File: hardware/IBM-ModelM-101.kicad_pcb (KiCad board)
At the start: 2 copper layers, 150 x 50 mm, 42 parts, among them J1 CONN-MOLEX-0670688000-USB-B, J2 KEYBOARD_ACTIVE_LINES, J3 KEYBOARD_INPUT_LINES, J4 CHASSIS_GROUND, J5 STATUS_LEDS, J6 DEBUG_FTDI, J7 JTAG, SW1 BOOT0, SW2 RESET, U1 TLV70233DBV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

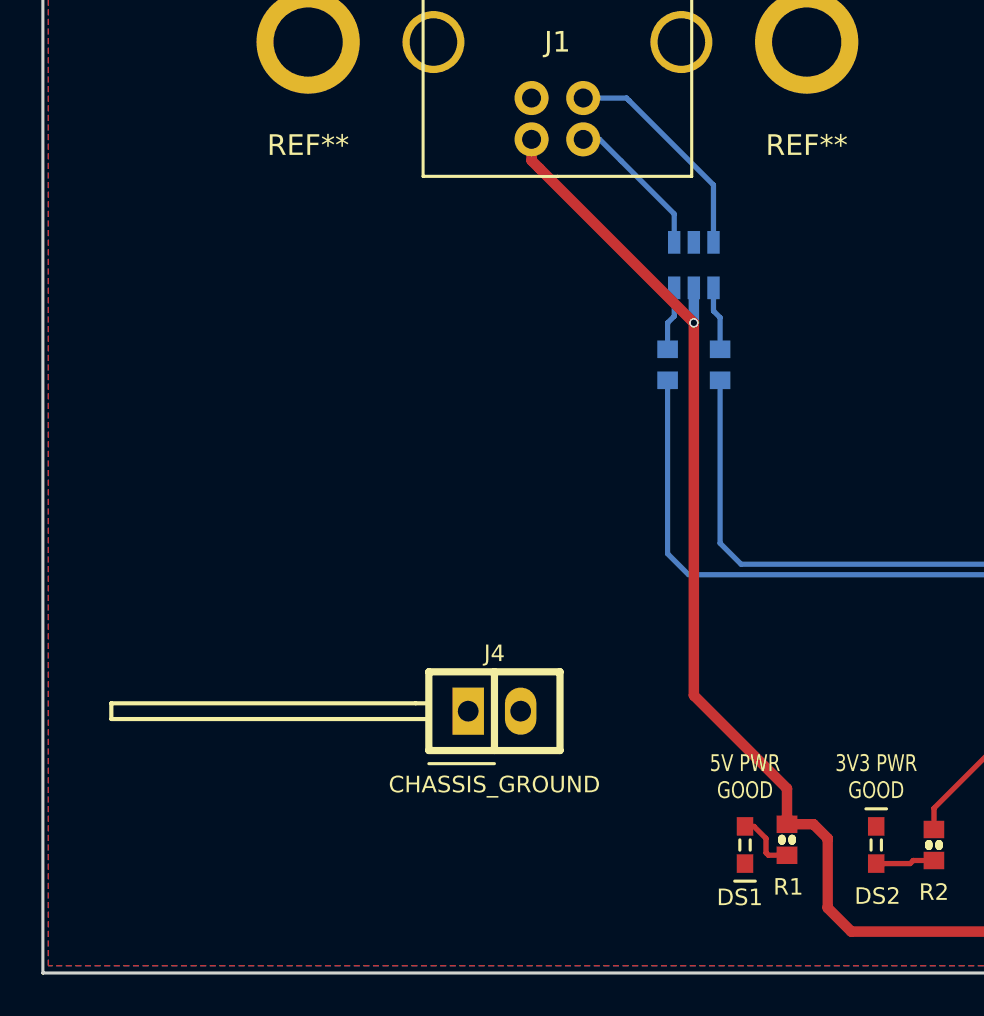
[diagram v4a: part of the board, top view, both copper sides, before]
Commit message: Updates + replaced tab header with correct footprint
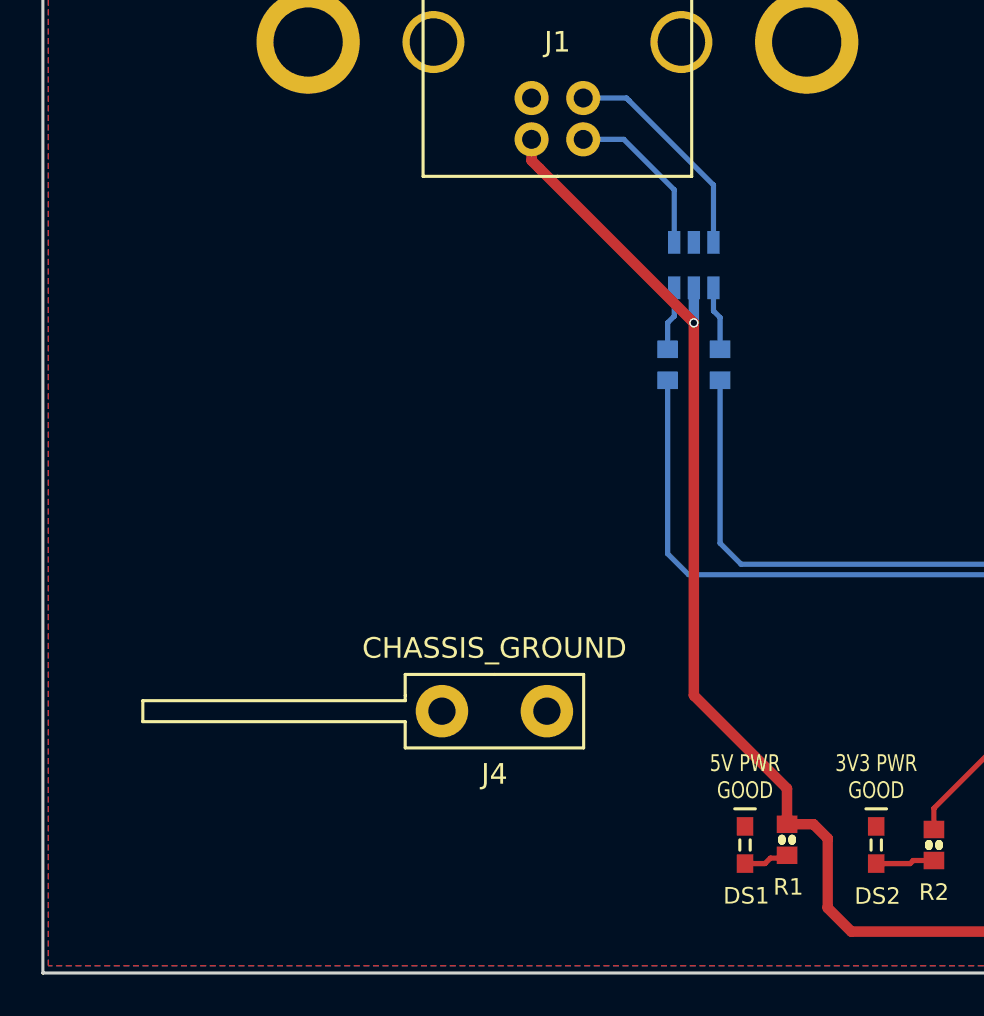
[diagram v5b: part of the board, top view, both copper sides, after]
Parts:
- J4: footprint conn-100mil:CONN-100MIL-M-1x2 -> conn-molex:CONN-MOLEX-0197134001-TAB
- turned DS1 to 270 degrees
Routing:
- net Net-(DS1-Pad2): track 3.02 -> 2.20 mm
- net Net-(DZ1-Pad1): track 7.27 -> 7.96 mm
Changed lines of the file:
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@@
     (links 128)
     (no_connects 1)
-    (area 85.003799 26.605199 235.153801 76.755201)
+    (area 85.003799 20.793999 235.153801 76.755201)
     (thickness 1.6)
-    (drawings 12)
-    (tracks 494)
+    (drawings 7)
+    (tracks 492)
     (zones 0)
     (modules 42)
@@
     (visible_elements 7FFFFFFF)
     (pcbplotparams
-      (layerselection 0x01030_80000001)
+      (layerselection 0x010f0_80000001)
       (usegerberextensions false)
       (excludeedgelayer true)
@@
   )
   (module smd-semi:LED-0603 (layer F.Cu)
-    (at 119.0625 70.485 90)
-    (fp_text reference DS1 (at -2.54 -0.254 180) (layer F.SilkS)
-      (effects (font (size 0.8 0.8) (thickness 0.15)))
-    )
-    (fp_text value 5V_PWR_GOOD (at -4.191 -1.4605 180) (layer F.Fab)
+    (at 119.0625 70.485 270)
+    (fp_text reference DS1 (at 2.4638 -0.0635 360) (layer F.SilkS)
+      (effects (font (size 0.8 0.8) (thickness 0.15)))
+    )
+    (fp_text value 5V_PWR_GOOD (at 4.2164 0.9779 360) (layer F.Fab)
       (effects (font (size 0.8 0.8) (thickness 0.15)))
     )
@@
     (fp_line (start 1.75 0.75) (end -1.75 0.75) (layer F.CrtYd) (width 0.15))
     (fp_line (start -1.75 0.75) (end -1.75 -0.75) (layer F.CrtYd) (width 0.15))
-    (pad 1 smd rect (at -0.89916 0 90) (size 0.89916 0.8001) (layers F.Cu F.Paste F.Mask)
-      (net 1 GND))
-    (pad 2 smd rect (at 0.89916 0 90) (size 0.89916 0.8001) (layers F.Cu F.Paste F.Mask)
+    (pad 1 smd rect (at -0.89916 0 270) (size 0.89916 0.8001) (layers F.Cu F.Paste F.Mask)
+      (net 1 GND))
+    (pad 2 smd rect (at 0.89916 0 270) (size 0.89916 0.8001) (layers F.Cu F.Paste F.Mask)
       (net 7 "Net-(DS1-Pad2)"))
     (model smd_leds/led_0603.wrl
@@
     )
   )
-  (module conn-100mil:CONN-100MIL-M-1x2 locked (layer F.Cu)
-    (at 106.934 64.008)
-    (fp_text reference J4 (at 0 -2.794) (layer F.SilkS)
-      (effects (font (size 0.8 0.8) (thickness 0.15)))
-    )
-    (fp_text value CHASSIS_GROUND (at 0 3.556) (layer F.SilkS)
-      (effects (font (size 0.8 0.8) (thickness 0.15)))
-    )
-    (fp_line (start -3.175 -1.905) (end 3.175 -1.905) (layer F.CrtYd) (width 0.15))
-    (fp_line (start 3.175 -1.905) (end 3.175 1.905) (layer F.CrtYd) (width 0.15))
-    (fp_line (start 3.175 1.905) (end -3.175 1.905) (layer F.CrtYd) (width 0.15))
-    (fp_line (start -3.175 1.905) (end -3.175 -1.905) (layer F.CrtYd) (width 0.15))
-    (fp_line (start -3.175 -1.905) (end 3.175 -1.905) (layer F.Fab) (width 0.15))
-    (fp_line (start 3.175 -1.905) (end 3.175 1.905) (layer F.Fab) (width 0.15))
-    (fp_line (start 3.175 1.905) (end -3.175 1.905) (layer F.Fab) (width 0.15))
-    (fp_line (start -3.175 1.905) (end -3.175 -1.905) (layer F.Fab) (width 0.15))
-    (fp_line (start -3.175 -1.905) (end 3.175 -1.905) (layer F.SilkS) (width 0.35))
-    (fp_line (start 3.175 -1.905) (end 3.175 1.905) (layer F.SilkS) (width 0.35))
-    (fp_line (start 3.175 1.905) (end -3.175 1.905) (layer F.SilkS) (width 0.35))
-    (fp_line (start -3.175 1.905) (end -3.175 -1.905) (layer F.SilkS) (width 0.35))
-    (fp_line (start 0 -1.905) (end 0 1.905) (layer F.SilkS) (width 0.35))
-    (fp_line (start 0 -1.905) (end 0 1.905) (layer F.Fab) (width 0.15))
-    (fp_line (start -3.175 2.54) (end 0 2.54) (layer F.SilkS) (width 0.15))
-    (pad 1 thru_hole rect (at -1.27 0) (size 1.524 2.286) (drill 1) (layers *.Cu *.Mask F.SilkS)
-      (net 1 GND))
-    (pad 2 thru_hole oval (at 1.27 0) (size 1.524 2.286) (drill 1) (layers *.Cu *.Mask F.SilkS)
-      (net 1 GND))
-    (model pin_strip/pin_strip_2.wrl
-      (at (xyz 0 0 0))
-      (scale (xyz 1 1 1))
-      (rotate (xyz 0 0 0))
-    )
-  )
   (module conn-100mil:CONN-100MIL-M-1x4-SHROUD (layer F.Cu)
     (at 225.79 53.89 270)
@@
   (module mech:PTH-3MM-PLUS (layer F.Cu)
     (at 122.047 31.623)
-    (fp_text reference REF** (at 0 5) (layer F.SilkS)
+    (fp_text reference REF** (at 0 5) (layer F.SilkS) hide
       (effects (font (size 1 1) (thickness 0.15)))
     )
@@
   (module mech:PTH-3MM-PLUS (layer F.Cu)
     (at 97.917 31.623)
-    (fp_text reference REF** (at 0 5) (layer F.SilkS)
+    (fp_text reference REF** (at 0 5) (layer F.SilkS) hide
       (effects (font (size 1 1) (thickness 0.15)))
     )
@@
       (net 3 +5V))
   )
+  (module conn-molex:CONN-MOLEX-0197134001-TAB locked (layer F.Cu)
+    (at 106.934 64.008)
+    (fp_text reference J4 (at 0 3.048) (layer F.SilkS)
+      (effects (font (size 1 1) (thickness 0.15)))
+    )
+    (fp_text value CHASSIS_GROUND (at 0 -3.048) (layer F.SilkS)
+      (effects (font (size 1 1) (thickness 0.15)))
+    )
+    (fp_line (start -4.318 -0.508) (end -17.018 -0.508) (layer F.SilkS) (width 0.15))
+    (fp_line (start -17.018 -0.508) (end -17.018 0.508) (layer F.SilkS) (width 0.15))
+    (fp_line (start -17.018 0.508) (end -4.318 0.508) (layer F.SilkS) (width 0.15))
+    (fp_line (start -4.318 -0.762) (end -4.318 -0.508) (layer F.SilkS) (width 0.15))
+    (fp_line (start 0 -1.778) (end -4.318 -1.778) (layer F.SilkS) (width 0.15))
+    (fp_line (start -4.318 -1.778) (end -4.318 -0.762) (layer F.SilkS) (width 0.15))
+    (fp_line (start -4.318 1.778) (end -4.318 0.508) (layer F.SilkS) (width 0.15))
+    (fp_line (start 0 -1.778) (end 4.318 -1.778) (layer F.SilkS) (width 0.15))
+    (fp_line (start 4.318 -1.778) (end 4.318 1.778) (layer F.SilkS) (width 0.15))
+    (fp_line (start 4.318 1.778) (end -4.318 1.778) (layer F.SilkS) (width 0.15))
+    (pad 1 thru_hole circle (at -2.54 0) (size 2.54 2.54) (drill 1.3208) (layers *.Cu *.Mask F.SilkS)
+      (net 1 GND))
+    (pad 2 thru_hole circle (at 2.54 0) (size 2.54 2.54) (drill 1.3208) (layers *.Cu *.Mask F.SilkS)
+      (net 1 GND))
+  )
   (gr_text "5V FROM\nJTAG\n" (at 162.6235 64.643) (layer F.SilkS)
     (effects (font (size 0.8128 0.889) (thickness 0.1524)))
@@
     (effects (font (size 0.8128 0.635) (thickness 0.1524)))
   )
-  (gr_line (start 103.124 64.389) (end 103.759 64.389) (angle 90) (layer F.SilkS) (width 0.2))
-  (gr_line (start 103.124 63.627) (end 103.759 63.627) (angle 90) (layer F.SilkS) (width 0.2))
-  (gr_line (start 103.124 63.627) (end 88.392 63.627) (angle 90) (layer F.SilkS) (width 0.2))
-  (gr_line (start 88.392 64.389) (end 103.124 64.389) (angle 90) (layer F.SilkS) (width 0.2))
-  (gr_line (start 88.392 63.627) (end 88.392 64.389) (angle 90) (layer F.SilkS) (width 0.2))
   (gr_line (start 85.0788 76.6802) (end 85.0788 26.6802) (angle 90) (layer Edge.Cuts) (width 0.15))
   (gr_line (start 235.0788 76.6802) (end 85.0788 76.6802) (angle 90) (layer Edge.Cuts) (width 0.15))
@@
   (segment (start 150.137 45.201) (end 149.987 45.351) (width 0.254) (layer F.Cu) (net 2))
   (segment (start 151.963 45.145) (end 152.019 45.201) (width 0.254) (layer F.Cu) (net 2))
-  (segment (start 108.732 36.333) (end 108.732 37.358) (width 0.508) (layer F.Cu) (net 3) (status 400000))
+  (segment (start 108.732 36.333) (end 108.732 37.358) (width 0.508) (layer F.Cu) (net 3))
   (segment (start 109.1184 37.7444) (end 116.586 45.212) (width 0.508) (layer F.Cu) (net 3))
   (segment (start 108.732 37.358) (end 109.1184 37.7444) (width 0.508) (layer F.Cu) (net 3))
@@
   (segment (start 176.022 60.706) (end 176.022 69.088) (width 0.254) (layer B.Cu) (net 6))
   (segment (start 176.022 60.706) (end 176.022 56.63) (width 0.254) (layer B.Cu) (net 6))
-  (segment (start 119.0625 69.58584) (end 119.49684 69.58584) (width 0.254) (layer F.Cu) (net 7))
-  (segment (start 120.1935 70.981) (end 121.0945 70.981) (width 0.254) (layer F.Cu) (net 7))
-  (segment (start 120.0785 70.866) (end 120.1935 70.981) (width 0.254) (layer F.Cu) (net 7))
-  (segment (start 120.0785 70.1675) (end 120.0785 70.866) (width 0.254) (layer F.Cu) (net 7))
-  (segment (start 119.49684 69.58584) (end 120.0785 70.1675) (width 0.254) (layer F.Cu) (net 7))
+  (segment (start 119.0625 71.38416) (end 120.03024 71.38416) (width 0.254) (layer F.Cu) (net 7))
+  (segment (start 120.2944 71.12) (end 120.9555 71.12) (width 0.254) (layer F.Cu) (net 7))
+  (segment (start 120.03024 71.38416) (end 120.2944 71.12) (width 0.254) (layer F.Cu) (net 7))
+  (segment (start 120.9555 71.12) (end 121.0945 70.981) (width 0.254) (layer F.Cu) (net 7))
   (segment (start 125.4125 71.38416) (end 127.05334 71.38416) (width 0.254) (layer F.Cu) (net 8))
   (segment (start 127.2025 71.235) (end 128.2065 71.235) (width 0.254) (layer F.Cu) (net 8))
   (segment (start 127.05334 71.38416) (end 127.2025 71.235) (width 0.254) (layer F.Cu) (net 8))
   (segment (start 125.26334 71.235) (end 125.4125 71.38416) (width 0.254) (layer F.Cu) (net 8))
-  (segment (start 111.232 36.333) (end 112.025 36.333) (width 0.254) (layer B.Cu) (net 9) (status C00000))
-  (segment (start 112.025 36.333) (end 113.0681 37.3761) (width 0.254) (layer B.Cu) (net 9) (status 400000))
-  (segment (start 115.636 39.944) (end 115.636 41.318) (width 0.254) (layer B.Cu) (net 9))
-  (segment (start 113.0681 37.3761) (end 115.636 39.944) (width 0.254) (layer B.Cu) (net 9))
+  (segment (start 115.636 41.318) (end 115.636 38.7756) (width 0.254) (layer B.Cu) (net 9))
+  (segment (start 113.1934 36.333) (end 111.232 36.333) (width 0.254) (layer B.Cu) (net 9))
+  (segment (start 115.636 38.7756) (end 113.1934 36.333) (width 0.254) (layer B.Cu) (net 9))
   (segment (start 111.232 34.333) (end 113.327 34.333) (width 0.254) (layer B.Cu) (net 10))
   (segment (start 113.454 34.46) (end 117.536 38.542) (width 0.254) (layer B.Cu) (net 10))

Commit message: Fixed unconnected pads + ground plane.
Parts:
- moved C5 3.07 mm to (162.3, 48.5), turned to 180 degrees
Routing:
- net GND: track 33.3 -> 40.4 mm, vias 1 -> 2
- net +3V3: track 205.6 -> 206.6 mm
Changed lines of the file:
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@@
   (general
     (links 128)
-    (no_connects 1)
+    (no_connects 0)
     (area 85.003799 20.793999 235.153801 76.755201)
     (thickness 1.6)
     (drawings 7)
-    (tracks 492)
+    (tracks 501)
     (zones 0)
     (modules 42)
@@
   )
   (module IPC7351-Nominal:CAPC1608X55 (layer F.Cu)
-    (at 159.258 48.895)
+    (at 162.306 48.514 180)
     (descr "Capacitor,non-polarized,Chip;1.60mm L X 0.80mm W X 0.55mm H")
     (attr smd)
-    (fp_text reference C5 (at -2.413 0.0635) (layer F.SilkS)
-      (effects (font (size 0.8 0.8) (thickness 0.15)))
-    )
-    (fp_text value 100nF (at 0 0) (layer F.Fab)
+    (fp_text reference C5 (at -2.413 0.0635 180) (layer F.SilkS)
+      (effects (font (size 0.8 0.8) (thickness 0.15)))
+    )
+    (fp_text value 100nF (at 0 0 180) (layer F.Fab)
       (effects (font (size 0.8 0.8) (thickness 0.15)))
     )
@@
     (fp_line (start 1.45 0.725) (end -1.45 0.725) (layer F.CrtYd) (width 0.15))
     (fp_line (start -1.45 0.725) (end -1.45 -0.725) (layer F.CrtYd) (width 0.15))
-    (pad 1 smd rect (at -0.75 0) (size 0.9 0.95) (layers F.Cu F.Paste F.Mask)
-      (net 1 GND))
-    (pad 2 smd rect (at 0.75 0) (size 0.9 0.95) (layers F.Cu F.Paste F.Mask)
+    (pad 1 smd rect (at -0.75 0 180) (size 0.9 0.95) (layers F.Cu F.Paste F.Mask)
+      (net 1 GND))
+    (pad 2 smd rect (at 0.75 0 180) (size 0.9 0.95) (layers F.Cu F.Paste F.Mask)
       (net 2 +3V3))
     (model smd_cap/c_0603.wrl
@@
       (effects (font (size 0.8 0.8) (thickness 0.15)) (justify mirror))
     )
-    (fp_text value STM32F102C6 (at 0 0 270) (layer B.Fab)
+    (fp_text value STM32F102C6 (at -21.59 -17.018 360) (layer B.Fab) hide
       (effects (font (size 0.8 0.8) (thickness 0.15)) (justify mirror))
     )
@@
   (gr_line (start 235.0788 26.6802) (end 235.0788 76.6802) (angle 90) (layer Edge.Cuts) (width 0.15))
   (gr_line (start 85.0788 26.6802) (end 235.0788 26.6802) (angle 90) (layer Edge.Cuts) (width 0.15))
+  (segment (start 159.766 49.022) (end 158.623 49.022) (width 0.254) (layer F.Cu) (net 1))
+  (segment (start 161.762 52.796) (end 159.766 50.8) (width 0.254) (layer B.Cu) (net 1))
+  (segment (start 159.766 50.8) (end 159.766 49.022) (width 0.254) (layer B.Cu) (net 1))
+  (via (at 159.766 49.022) (size 0.4572) (drill 0.3048) (layers F.Cu B.Cu) (net 1))
+  (segment (start 162.95 52.796) (end 161.762 52.796) (width 0.254) (layer B.Cu) (net 1))
+  (segment (start 158.623 49.022) (end 158.496 48.895) (width 0.254) (layer F.Cu) (net 1))
   (segment (start 156.5 54.746) (end 156.5 55.5265) (width 0.254) (layer B.Cu) (net 1))
   (segment (start 134.851 55.6665) (end 134.851 54.864) (width 0.254) (layer F.Cu) (net 1))
@@
   (segment (start 149.987 46.851) (end 151.869 46.851) (width 0.254) (layer F.Cu) (net 1))
   (segment (start 151.869 46.851) (end 152.019 47.001) (width 0.254) (layer F.Cu) (net 1))
-  (segment (start 158.508 48.895) (end 153.913 48.895) (width 0.254) (layer F.Cu) (net 1))
+  (segment (start 158.508 48.895) (end 158.496 48.895) (width 0.254) (layer F.Cu) (net 1))
+  (segment (start 158.496 48.895) (end 153.913 48.895) (width 0.254) (layer F.Cu) (net 1))
   (segment (start 153.913 48.895) (end 152.019 47.001) (width 0.254) (layer F.Cu) (net 1))
+  (segment (start 161.556 48.514) (end 160.528 48.514) (width 0.254) (layer F.Cu) (net 2))
+  (segment (start 160.02 48.26) (end 160.02 47.752) (width 0.254) (layer F.Cu) (net 2))
+  (segment (start 160.274 48.514) (end 160.02 48.26) (width 0.254) (layer F.Cu) (net 2))
+  (segment (start 160.528 48.514) (end 160.274 48.514) (width 0.254) (layer F.Cu) (net 2))
   (segment (start 148.336 55.8165) (end 147.8915 55.8165) (width 0.254) (layer F.Cu) (net 2))
   (segment (start 153.2255 55.8165) (end 148.336 55.8165) (width 0.254) (layer B.Cu) (net 2))
@@
   (segment (start 153.924 70.104) (end 153.924 72.898) (width 0.254) (layer F.Cu) (net 2))
   (segment (start 145.415 61.595) (end 153.924 70.104) (width 0.254) (layer F.Cu) (net 2))
-  (segment (start 160.02 47.752) (end 160.02 48.883) (width 0.254) (layer F.Cu) (net 2))
-  (segment (start 160.02 48.883) (end 160.008 48.895) (width 0.254) (layer F.Cu) (net 2))
   (segment (start 154.559 46.355) (end 158.623 46.355) (width 0.254) (layer F.Cu) (net 2))
   (segment (start 160 47.732) (end 160 46.346) (width 0.254) (layer B.Cu) (net 2))
@@
     (polygon
       (pts
-        (xy 234.696 76.327) (xy 85.344 76.327) (xy 85.344 26.797) (xy 234.95 26.797) (xy 234.696 76.327)
+        (xy 234.696 76.327) (xy 85.471 76.327) (xy 85.471 27.051) (xy 234.696 27.051) (xy 234.696 76.327)
       )
     )
     (polygon
       (pts        (xy 135.382 62.738) (xy 135.382 71.882) (xy 137.16 71.882) (xy 137.16 62.738) (xy 135.382 62.738)
-      )
-    )
-  )
-  (zone (net 1) (net_name GND) (layer B.Cu) (hatch edge 0.508)
-    (connect_pads (clearance 0.127))
-    (min_thickness 0.2032)
-    (fill yes (arc_segments 16) (thermal_gap 0.1524) (thermal_bridge_width 0.254))
-    (polygon
-      (pts
-        (xy 234.696 76.327) (xy 85.344 76.327) (xy 85.344 26.797) (xy 234.95 26.797) (xy 234.696 76.327)
       )
     )
@@
       )
     )
+  )
+  (zone (net 1) (net_name GND) (layer B.Cu) (hatch edge 0.508)
+    (connect_pads (clearance 0.127))
+    (min_thickness 0.2032)
+    (fill yes (arc_segments 16) (thermal_gap 0.1524) (thermal_bridge_width 0.254))
+    (polygon
+      (pts
+        (xy 234.696 76.327) (xy 85.471 76.327) (xy 85.471 27.051) (xy 234.696 27.051) (xy 234.696 76.327)
+      )
+    )
+    (polygon
+      (pts        (xy 135.382 62.738) (xy 135.382 71.882) (xy 137.16 71.882) (xy 137.16 62.738) (xy 135.382 62.738)
+      )
+    )

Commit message: Added artwork and logo
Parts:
- added G***: LOGO, hardware:IBM-Model-M-Neg, F.Cu at (101.0, 49.0)
- added G***: LOGO, hardware:ModelMUsb, F.Cu at (199.0, 50.0)
